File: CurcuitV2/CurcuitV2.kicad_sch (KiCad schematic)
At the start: 0 parts

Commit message: 必要な部品の挿入ほぼ完了
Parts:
- added C1, C2, C3, C4, C5, C6, C7, C8: 10u, Capacitor_SMD:C_0805_2012Metric, symbol Device:C
- added C10, C11, C26, C9: 0.1u, Capacitor_SMD:C_0603_1608Metric, symbol Device:C
- added D4: D_Schottky, Diode_SMD:D_SOD-323_HandSoldering, symbol Device:D_Schottky
- added IC1: AS5600-ASOT, Package_SO:SOIC-8_3.9x4.9mm_P1.27mm, symbol AS5600-ASOT:AS5600-ASOT
- added J1: Conn_01x07, Connector_PinSocket_2.54mm:PinSocket_1x07_P2.54mm_Vertical, symbol Connector_Generic:Conn_01x07
- added J2: Conn_01x03, Connector_JST:JST_XH_S3B-XH-A_1x03_P2.50mm_Horizontal, symbol Connector_Generic:Conn_01x03
- added J3: Conn_01x02, Connector_JST:JST_XH_S2B-XH-A_1x02_P2.50mm_Horizontal, symbol Connector_Generic:Conn_01x02
- added Q1, Q2, Q3, Q4, Q5, Q6: Q_NMOS_DGS, 0-MyLibrary:SSM6K819R, symbol Device:Q_NMOS_DGS
- added R1, R10, R2, R5, R6, R9: 10, Resistor_SMD:R_0603_1608Metric, symbol Device:R
- added R11, R12, R13, R14, R3, R4, R7, R8: 10k, Resistor_SMD:R_0603_1608Metric, symbol Device:R
- added SW1, SW2: SW_Push, Button_Switch_SMD:SW_Push_1P1T_NO_Vertical_Wuerth_434133025816, symbol Switch:SW_Push
- added U1: DRV8300DPWR, Package_SO:TSSOP-20_4.4x6.5mm_P0.65mm, symbol 0-MyLibrary:DRV8300DPWR
- added U2: STM32F303K8Tx, Package_QFP:LQFP-32_7x7mm_P0.8mm, symbol MCU_ST_STM32F3:STM32F303K8Tx
- added U7: AP7375-3.3, Package_TO_SOT_SMD:SOT-23, symbol Regulator_Linear:APE8865NR-15-HF-3
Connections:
- new net: Q3.2 (G), R5.2, R7.1
- new net: Q2.2 (G), R2.2, R3.1
- new net: Q4.2 (G), R6.2, R8.1
- new net: Q6.2 (G), R10.2, R12.1
- new net: Q5.2 (G), R11.1, R9.2
- new net: Q1.2 (G), R1.2, R4.1
- new net: R13.1, U2.31 (BOOT0)
- new net +3V3: C10.2, C11.2, C26.2, C7.1, C9.2, D4.2 (A), IC1.1 (VDD5V), IC1.2 (VDD3V3), J1.2 (Pin_2), SW2.2, U2.1 (VDD), U2.17 (VDD), U2.5 (VDDA), U7.2 (VO)
- new net BSTA: C1.2, U1.20 (BSTA)
- new net BSTB: C2.2, U1.17 (BSTB)
- new net BSTC: C3.2, U1.14 (BSTC)
- new net BUTTON: R14.1, SW2.1
- new net ENCODER_OUT: IC1.3 (OUT)
- new net GHA: R1.1, U1.19 (GHA)
- new net GHB: R5.1, U1.16 (GHB)
- new net GHC: R9.1, U1.13 (GHC)
- new net GLA: R2.1, U1.11 (GLA)
- new net GLB: R6.1, U1.10 (GLB)
- new net GLC: R10.1, U1.9 (GLC)
- new net GND: C10.1, C11.1, C26.1, C4.2, C5.2, C6.2, C7.2, C8.2, C9.1, IC1.4 (GND), J1.1 (Pin_1), J3.1 (Pin_1), Q2.3 (S), Q4.3 (S), Q6.3 (S), R12.2, R13.2, R14.2, R3.2, R8.2, SW1.1, U1.8 (GND), U2.16 (VSS), U2.32 (VSS), U7.3 (GND)
- new net INHA: U1.1 (INHA)
- new net INHB: U1.2 (INHB)
- new net INHC: U1.3 (INHC)
- new net INLA: U1.4 (INLA)
- new net INLB: U1.5 (INLB)
- new net INLC: U1.6 (INLC)
- new net NSRT: J1.5 (Pin_5), SW1.2, U2.4 (NRST)
- new net OUTA: C1.1, J2.3 (Pin_3), Q1.3 (S), Q2.1 (D), R4.2, U1.18 (SHA)
- new net OUTB: C2.1, J2.2 (Pin_2), Q3.3 (S), Q4.1 (D), R7.2, U1.15 (SHB)
- new net OUTC: C3.1, J2.1 (Pin_1), Q5.3 (S), Q6.1 (D), R11.2, U1.12 (SHC)
- new net PC_RX: J1.7 (Pin_7)
- new net PC_TX: J1.6 (Pin_6)
- new net SWCLK: J1.4 (Pin_4), U2.24 (PA14)
- new net SWDIO: J1.3 (Pin_3), U2.23 (PA13)
- new net VCC: C4.1, C5.1, C6.1, C8.1, D4.1 (K), J3.2 (Pin_2), Q1.1 (D), Q3.1 (D), Q5.1 (D), U1.7 (GVDD), U7.1 (VI)

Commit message: CubeMX生成
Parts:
- added J4: Conn_01x02, Connector_JST:JST_PH_S2B-PH-K_1x02_P2.00mm_Horizontal, symbol Connector_Generic:Conn_01x02
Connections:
- net INHA: now also U2.20 (PA10)
- net INHB: now also U2.19 (PA9)
- net INHC: now also U2.18 (PA8)
- net INLA: now also U2.15 (PB1)
- net INLB: now also U2.14 (PB0)
- net INLC: now also U2.13 (PA7)
- net PC_RX: now also U2.30 (PB7)
- net PC_TX: now also U2.29 (PB6)

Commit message: ほぼ完成
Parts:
- added C12, C13, C14, C15, C16, C17, C18, C19, C20, C21, C23: 0.1u, Capacitor_SMD:C_0805_2012Metric, symbol Device:C
- added C22: 0.1u, Capacitor_SMD:C_0603_1608Metric, symbol Device:C
- added D1, D11, D12, D2, D3, D5: 1N4148W, Diode_SMD:D_SOD-123, symbol Diode:1N4148W
- added D10, D6, D7, D8, D9: LED, LED_SMD:LED_0603_1608Metric, symbol Device:LED
- added H1, H2, H3, H4: MountingHole_Pad, MountingHole:MountingHole_3.2mm_M3_ISO14580_Pad_TopBottom, symbol Mechanical:MountingHole_Pad
- added R15, R16, R17, R18, R19: 1k, Resistor_SMD:R_0603_1608Metric, symbol Device:R
- added R20: 10k, Resistor_SMD:R_0603_1608Metric, symbol Device:R
- added TP1, TP2, TP3, TP4, TP5: TestPoint, TestPoint:TestPoint_Pad_D2.5mm, symbol Connector:TestPoint
- added U3: MCP9700x-ETT, Package_TO_SOT_SMD:SOT-23, symbol Sensor_Temperature:MCP9700x-ETT
- added Y2: CSTNE16M0V530000R0, Crystal:Resonator_SMD_Murata_CSTxExxV-3Pin_3.0x1.1mm, symbol CSTNE16M0V530000R0:CSTNE16M0V530000R0
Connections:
- net +3V3: now also R20.2, U3.1 (V_{DD})
- net BUTTON: now also U2.6 (PA0)
- net ENCODER_OUT: now also U2.11 (PA5)
- net GND: now also D6.1 (K), D7.1 (K), D8.1 (K), D9.1 (K), H3.1, H4.1, U3.3 (GND), Y2.2; no longer C4.2, C5.2, C6.2, J3.1 (Pin_1), Q2.3 (S), Q4.3 (S), Q6.3 (S), R12.2, R3.2, R8.2, U1.8 (GND)
- net OUTA: now also D1.2 (A), D2.1 (K), TP1.1
- net OUTB: now also D3.2 (A), D5.1 (K), TP2.1
- net OUTC: now also D11.2 (A), D12.1 (K), TP3.1
- net VCC: now also C12.2, C13.2, C14.2, C15.2, C16.2, C17.2, C18.2, C19.2, C20.2, C21.2, C22.2, C23.2, D1.1 (K), D11.1 (K), D3.1 (K), R19.2, TP4.1
- net UART2_TX: now reaches J4.1 (Pin_1)
- net UART2_TX: now also U2.8 (PA2)
- net UART2_RX: now reaches J4.2 (Pin_2)
- net UART2_RX: now also U2.9 (PA3), R20.1
- net TEMP: now reaches U2.10 (PA4)
- net TEMP: now also U3.2 (V_{OUT})
- net at U2.2 (PF0): now also Y2.1
- net LED1: now reaches U2.25 (PA15)
- net LED1: now also R15.2
- net LED2: now reaches U2.26 (PB3)
- net LED2: now also R16.2
- net LED3: now reaches U2.27 (PB4)
- net LED3: now also R17.2
- net LED4: now reaches U2.28 (PB5)
- net LED4: now also R18.2
- net at U2.3 (PF1): now also Y2.3
- new net: D7.2 (A), R16.1
- new net: D8.2 (A), R17.1
- new net: D10.2 (A), R19.1
- new net: D6.2 (A), R15.1
- new net: D9.2 (A), R18.1
- new net GNDA: C12.1, C13.1, C14.1, C15.1, C16.1, C17.1, C18.1, C19.1, C20.1, C21.1, C22.1, C23.1, C4.2, C5.2, C6.2, D10.1 (K), D12.2 (A), D2.2 (A), D5.2 (A), H1.1, H2.1, J3.1 (Pin_1), Q2.3 (S), Q4.3 (S), Q6.3 (S), R12.2, R3.2, R8.2, TP5.1, U1.8 (GND)
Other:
- moved on the sheet: C4, C5, C6

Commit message: 完成
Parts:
- added NT1: NetTie_2, NetTie:NetTie-2_SMD_Pad2.0mm, symbol Device:NetTie_2
- added R21: 10k, Resistor_SMD:R_0603_1608Metric, symbol Device:R
- added R22: 1k, Resistor_SMD:R_0603_1608Metric, symbol Device:R
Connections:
- net GND: now also NT1.1, R22.1
- net GNDA: now also NT1.2
- net VCC: now also R21.2
- net VOLTAGE: now reaches U2.12 (PA6)
- net VOLTAGE: now also R21.1, R22.2
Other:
- moved on the sheet: C1, C10, C11, C12, C13, C14, C15, C16, C17, C18, C19, C2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

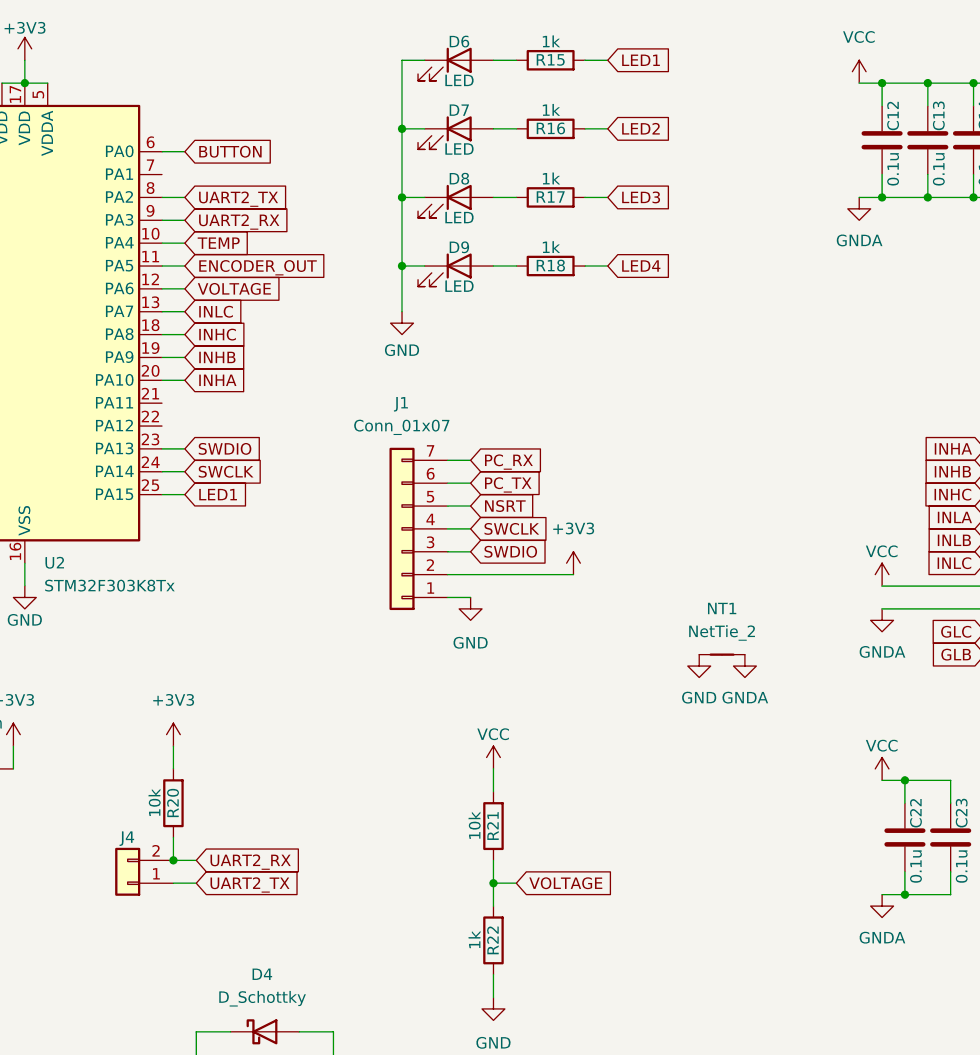
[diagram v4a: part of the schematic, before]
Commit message: 理想ダイオードの追加
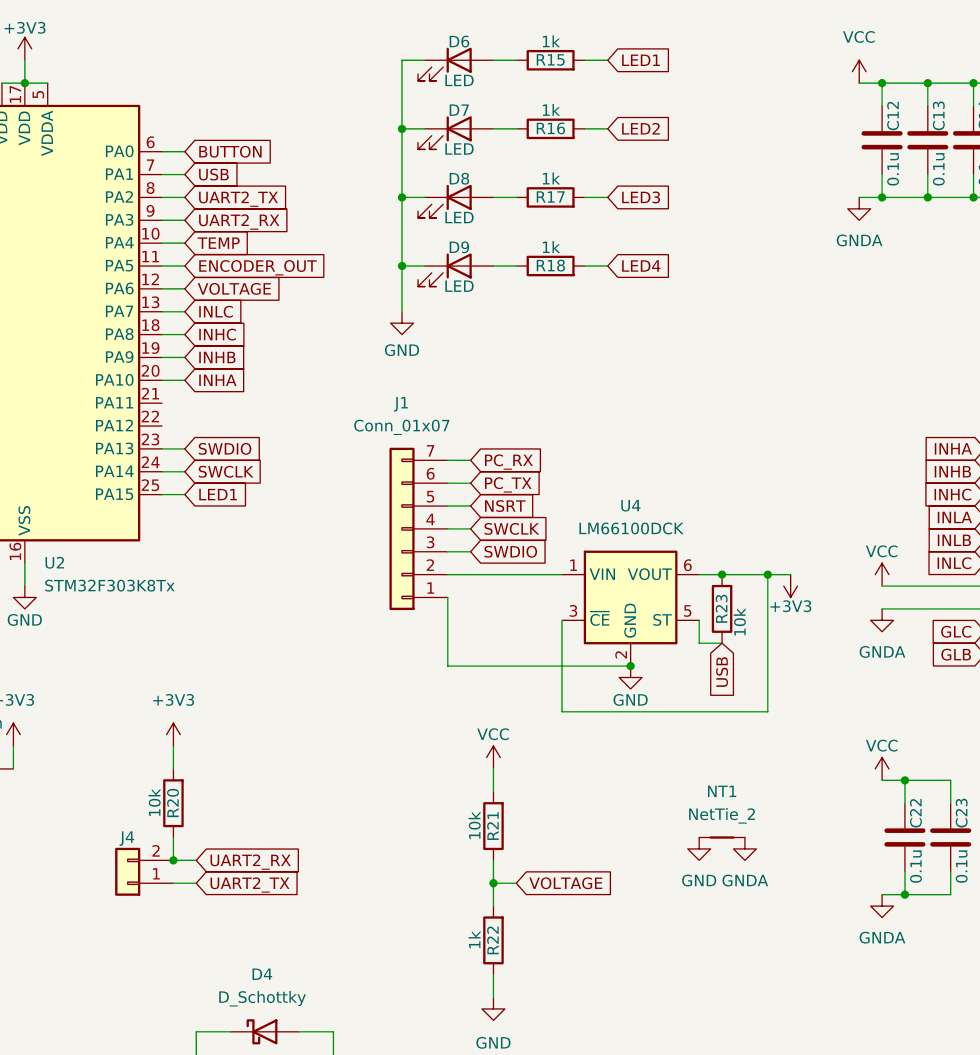
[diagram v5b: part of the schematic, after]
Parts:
- added R23: 10k, Resistor_SMD:R_0603_1608Metric, symbol Device:R
- added U4: LM66100DCK, Package_TO_SOT_SMD:SOT-363_SC-70-6, symbol Power_Management:LM66100DCK
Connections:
- net +3V3: now also R23.2, U4.3 (~{CE}), U4.6 (VOUT); no longer J1.2 (Pin_2)
- net GND: now also U4.2 (GND)
- net USB: now reaches U2.7 (PA1)
- net USB: now also R23.1, U4.5 (ST)
- new net: J1.2 (Pin_2), U4.1 (VIN)
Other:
- moved on the sheet: NT1

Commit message: シルクの追加
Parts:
- R19: value 1k -> 10k
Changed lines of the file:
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@@
 			)
 		)
-		(property "Value" "1k"
+		(property "Value" "10k"
 			(at 59.69 138.938 90)
 			(effects
